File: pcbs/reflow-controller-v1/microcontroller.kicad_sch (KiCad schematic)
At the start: 15 parts, among them J3 SWD, J4 UART, U3 STM32G474VETx

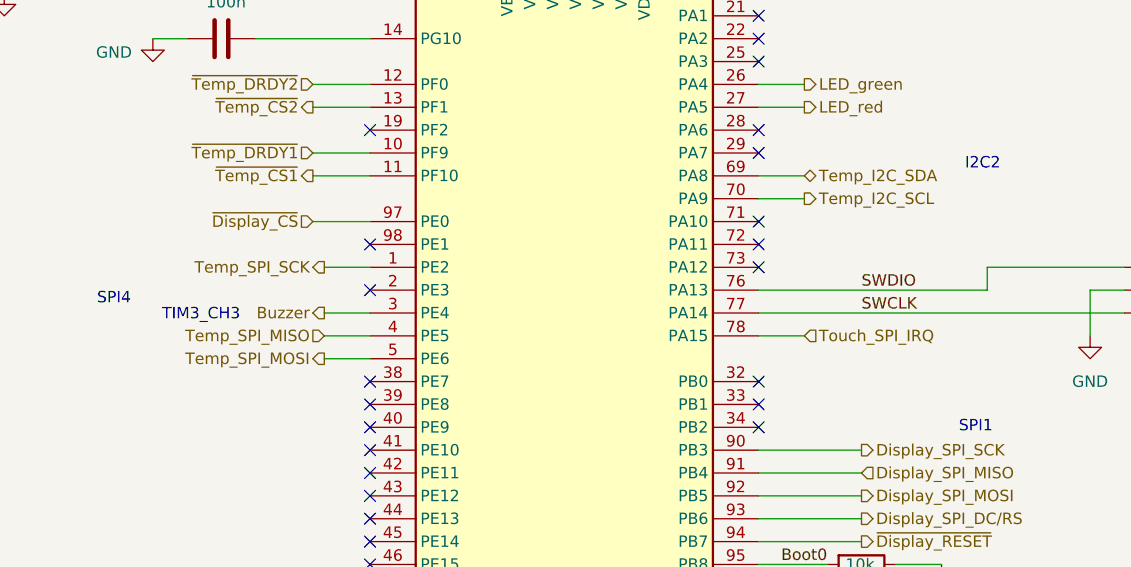
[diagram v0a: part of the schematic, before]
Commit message: move beeper
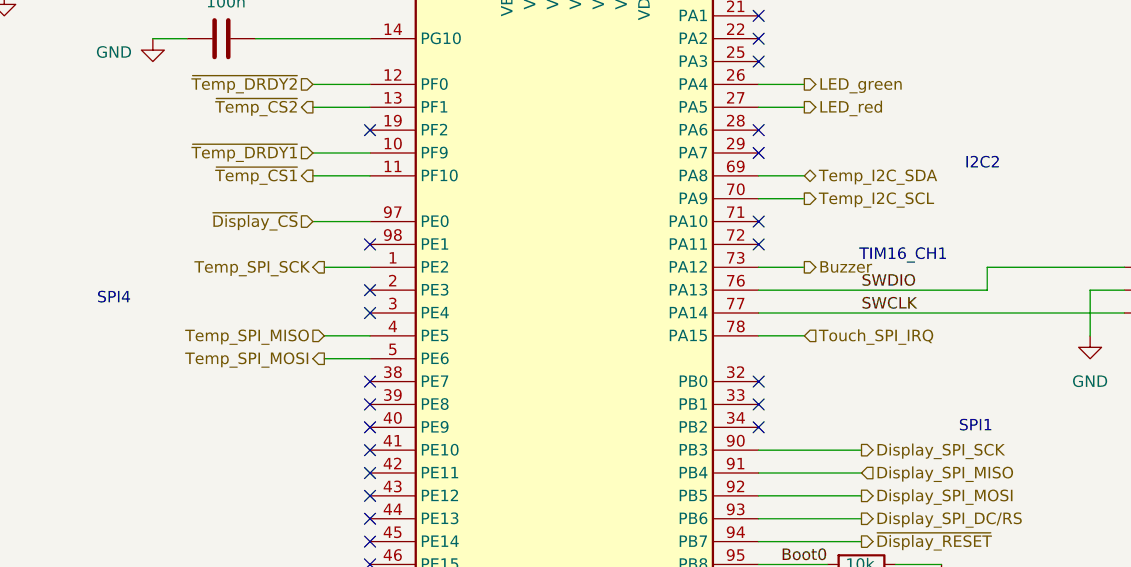
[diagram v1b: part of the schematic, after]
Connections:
- net Buzzer: now also U3.73 (PA12); no longer U3.3 (PE4)
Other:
- note added: "TIM16_CH1"
- note removed: "TIM3_CH3"
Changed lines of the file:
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@@
 	)
 	(no_connect
-		(at 144.78 69.85)
+		(at 101.6 74.93)
 	)
 	(no_connect
@@
 	(wire
 		(pts
-			(xy 96.52 74.93) (xy 101.6 74.93)
-		)
-		(stroke
-			(width 0)
-			(type default)
-		)
-	)
-	(wire
-		(pts
 			(xy 114.3 31.75) (xy 116.84 31.75)
 		)
@@
 	(wire
 		(pts
+			(xy 144.78 69.85) (xy 149.86 69.85)
+		)
+		(stroke
+			(width 0)
+			(type default)
+		)
+	)
+	(wire
+		(pts
 			(xy 101.6 140.97) (xy 93.98 140.97)
 		)
@@
 		)
 	)
-	(text "TIM3_CH3"
-		(exclude_from_sim no)
-		(at 78.486 75.184 0)
+	(text "TIM16_CH1"
+		(exclude_from_sim no)
+		(at 155.956 68.58 0)
 		(effects
 			(font
@@
 	(hierarchical_label "Buzzer"
 		(shape output)
-		(at 96.52 74.93 180)
-		(fields_autoplaced yes)
-		(effects
-			(font
-				(size 1.27 1.27)
-			)
-			(justify right)
-		)
-	)
+		(at 149.86 69.85 0)
+		(fields_autoplaced yes)
+		(effects
+			(font
+				(size 1.27 1.27)
+			)
+			(justify left)
+		)
+	)

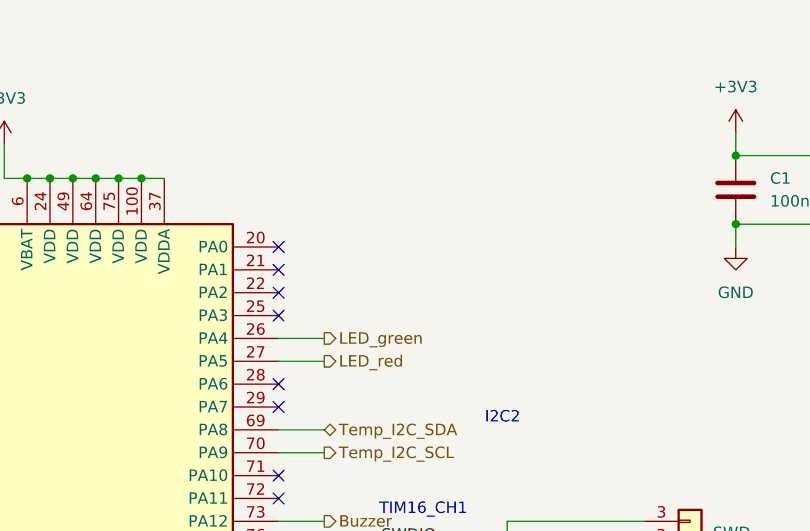
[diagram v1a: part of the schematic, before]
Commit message: add zero crossing detector
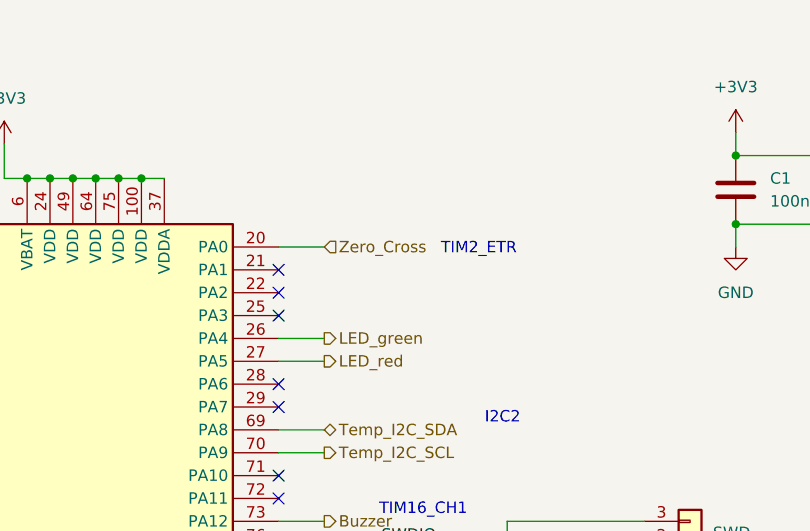
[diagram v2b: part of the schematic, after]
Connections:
- net Zero_Cross: now reaches U3.20 (PA0)
- no-connect marks 34 -> 33
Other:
- note added: "TIM2_ETR"
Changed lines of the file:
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@@
-	)
-	(no_connect
-		(at 144.78 39.37)
 	)
 	(no_connect
@@
 	(wire
 		(pts
+			(xy 144.78 39.37) (xy 149.86 39.37)
+		)
+		(stroke
+			(width 0)
+			(type default)
+		)
+	)
+	(wire
+		(pts
 			(xy 144.78 100.33) (xy 156.21 100.33)
 		)
@@
 				(size 1.27 1.27)
 			)
+		)
+	)
+	(text "TIM2_ETR"
+		(exclude_from_sim no)
+		(at 162.814 39.624 0)
+		(effects
+			(font
+				(size 1.27 1.27)
+			)
+			(justify left)
 		)
 	)
@@
 		)
 	)
+	(hierarchical_label "Zero_Cross"
+		(shape input)
+		(at 149.86 39.37 0)
+		(fields_autoplaced yes)
+		(effects
+			(font
+				(size 1.27 1.27)
+			)
+			(justify left)
+		)
+	)

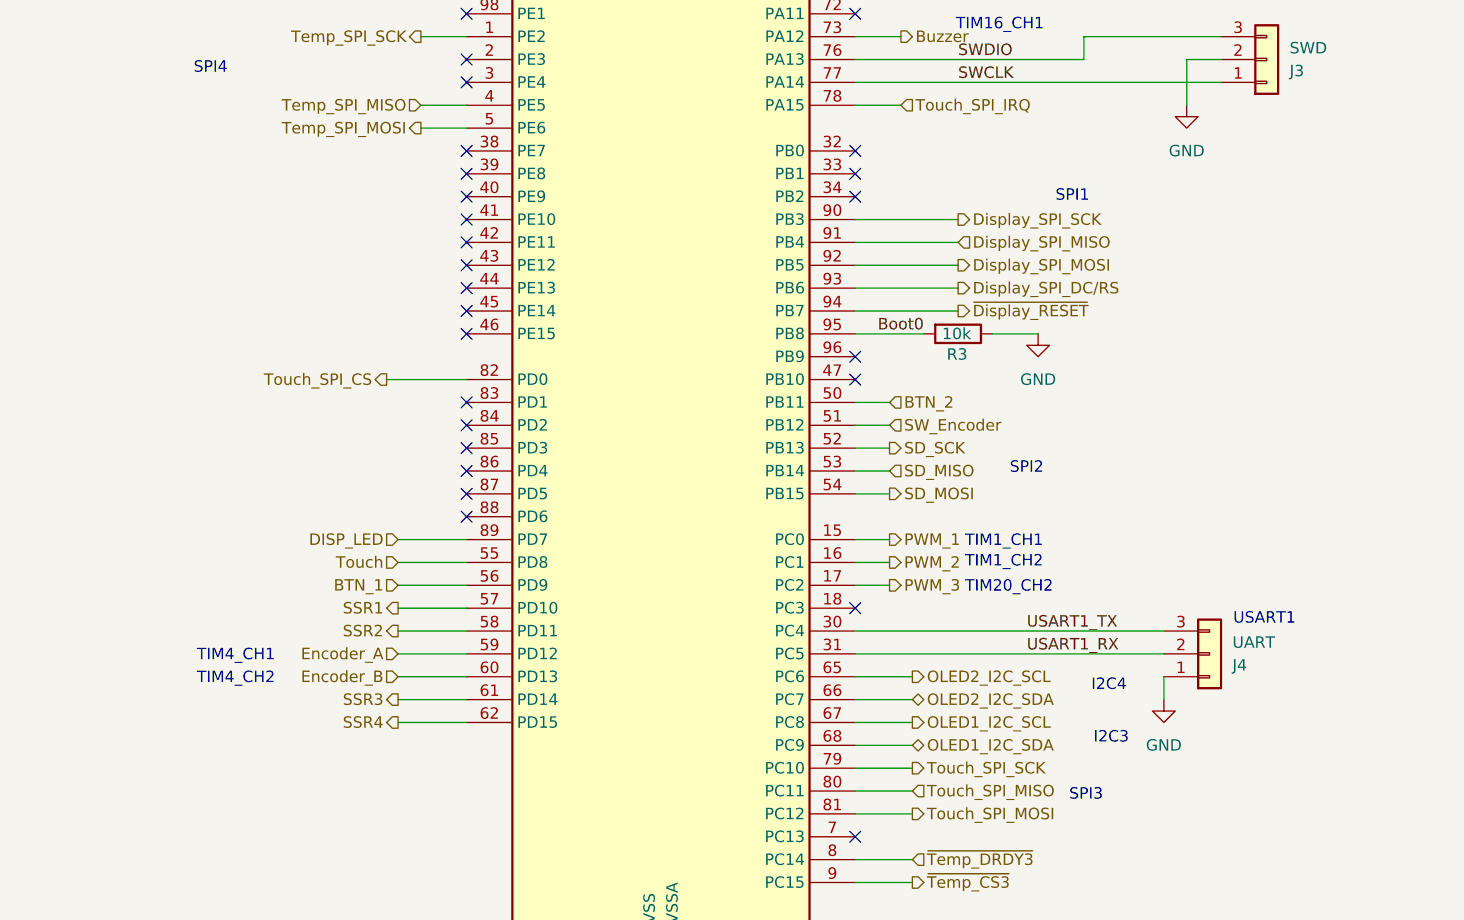
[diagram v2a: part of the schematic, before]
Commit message: update pcb size&display positioning
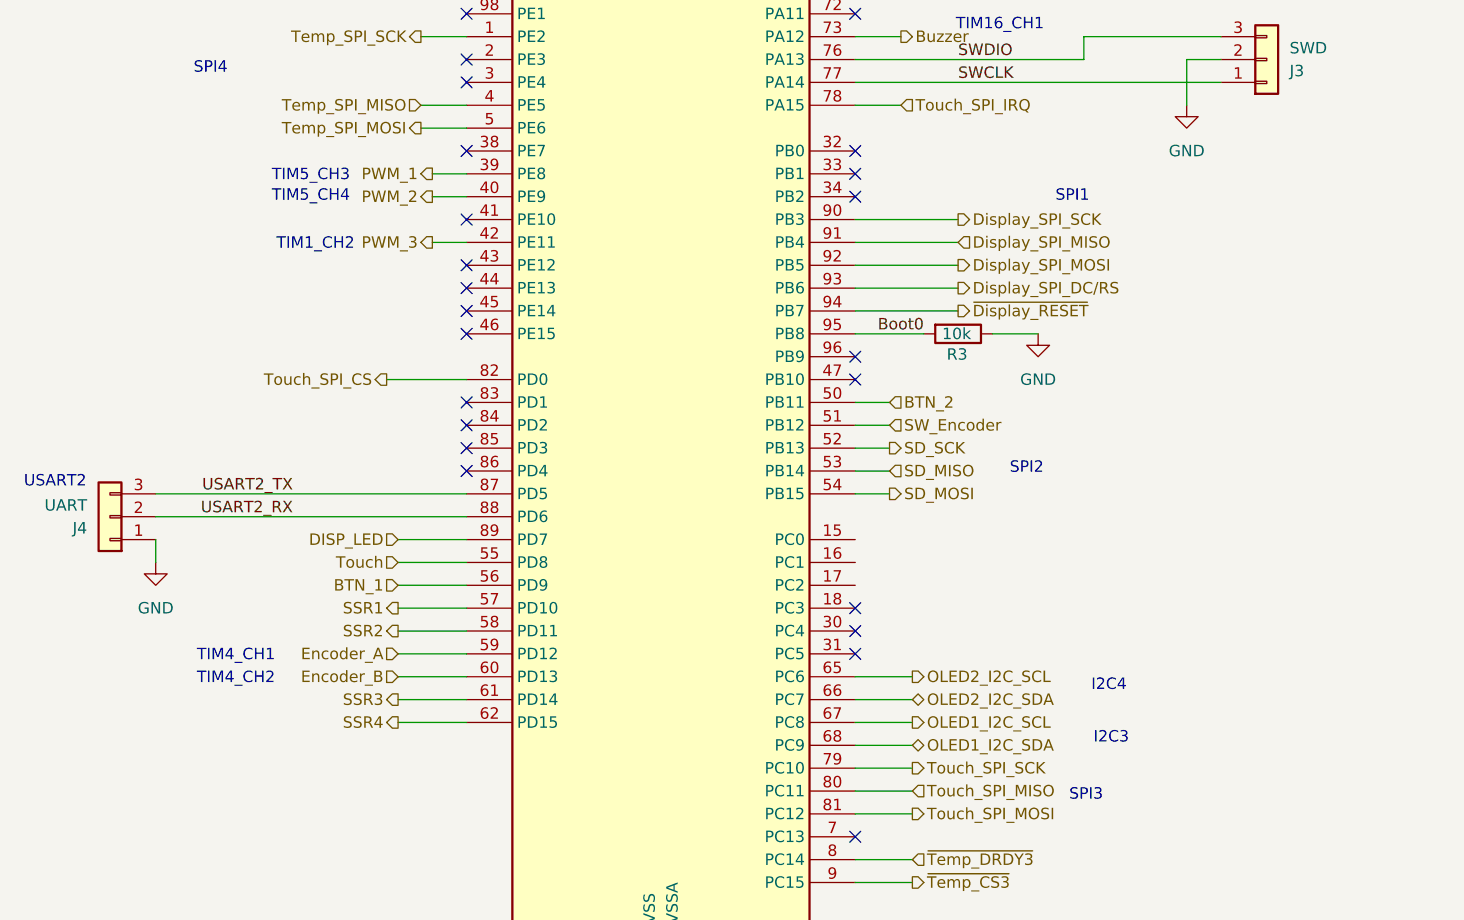
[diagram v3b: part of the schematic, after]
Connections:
- net PWM_1: now also U3.39 (PE8); no longer U3.15 (PC0)
- net PWM_2: now also U3.40 (PE9); no longer U3.16 (PC1)
- net PWM_3: now also U3.42 (PE11); no longer U3.17 (PC2)
- net USART2_TX: now reaches U3.87 (PD5)
- net USART2_TX: now also J4.3 (Pin_3)
- net USART2_RX: now reaches U3.88 (PD6)
- net USART2_RX: now also J4.2 (Pin_2)
- net USART1_RX: no longer names the net of U3.31 (PC5)
- net USART1_RX: no longer J4.2 (Pin_2)
- net USART1_TX: no longer names the net of U3.30 (PC4)
- net USART1_TX: no longer J4.3 (Pin_3)
- no-connect marks 33 -> 30
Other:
- note added: "TIM5_CH3"
- note added: "TIM5_CH4"
- note added: "USART2"
- note removed: "TIM1_CH1"
- note removed: "TIM20_CH2"
- note removed: "USART1"
- moved on the sheet: J4
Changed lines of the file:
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@@
-	)
-	(no_connect
-		(at 101.6 123.19)
 	)
 	(no_connect
@@
 	)
 	(no_connect
-		(at 101.6 85.09)
-	)
-	(no_connect
 		(at 101.6 100.33)
 	)
@@
 	)
 	(no_connect
-		(at 101.6 120.65)
-	)
-	(no_connect
 		(at 144.78 54.61)
 	)
@@
 	)
 	(no_connect
-		(at 101.6 92.71)
-	)
-	(no_connect
 		(at 144.78 46.99)
 	)
 	(no_connect
-		(at 101.6 87.63)
-	)
-	(no_connect
 		(at 144.78 107.95)
 	)
 	(no_connect
+		(at 144.78 135.89)
+	)
+	(no_connect
 		(at 101.6 82.55)
 	)
@@
 	)
 	(no_connect
+		(at 144.78 138.43)
+	)
+	(no_connect
 		(at 101.6 115.57)
 	)
@@
 	(wire
 		(pts
-			(xy 144.78 138.43) (xy 179.07 138.43)
+			(xy 67.056 123.19) (xy 101.6 123.19)
 		)
 		(stroke
@@
 	(wire
 		(pts
-			(xy 144.78 128.27) (xy 148.59 128.27)
+			(xy 101.6 87.63) (xy 97.79 87.63)
 		)
 		(stroke
@@
 	(wire
 		(pts
-			(xy 144.78 135.89) (xy 179.07 135.89)
+			(xy 67.056 120.65) (xy 101.6 120.65)
 		)
 		(stroke
@@
 	(wire
 		(pts
-			(xy 179.07 140.97) (xy 179.07 143.51)
+			(xy 67.056 125.73) (xy 67.056 128.27)
 		)
 		(stroke
@@
 	(wire
 		(pts
-			(xy 144.78 125.73) (xy 148.59 125.73)
+			(xy 101.6 85.09) (xy 97.79 85.09)
 		)
 		(stroke
@@
 	(wire
 		(pts
-			(xy 144.78 130.81) (xy 148.59 130.81)
+			(xy 101.6 92.71) (xy 97.79 92.71)
 		)
 		(stroke
@@
 		)
 	)
-	(text "TIM1_CH1"
+	(text "TIM5_CH3"
 		(exclude_from_sim no)
-		(at 156.972 125.984 0)
-		(effects
-			(font
-				(size 1.27 1.27)
-			)
-			(justify left)
+		(at 88.646 85.344 0)
+		(effects
+			(font
+				(size 1.27 1.27)
+			)
+			(justify right)
 		)
 	)
@@
 		)
 	)
-	(text "USART1"
+	(text "USART2"
 		(exclude_from_sim no)
-		(at 190.246 134.62 0)
-		(effects
-			(font
-				(size 1.27 1.27)
-			)
+		(at 55.88 119.38 0)
+		(effects
+			(font
+				(size 1.27 1.27)
+			)
+		)
+	)
+	(text "TIM5_CH4"
+		(exclude_from_sim no)
+		(at 88.646 87.63 0)
+		(effects
+			(font
+				(size 1.27 1.27)
+			)
+			(justify right)
 		)
 	)
 	(text "TIM1_CH2"
 		(exclude_from_sim no)
-		(at 156.972 128.27 0)
-		(effects
-			(font
-				(size 1.27 1.27)
-			)
-			(justify left)
-		)
-	)
-	(text "TIM20_CH2"
-		(exclude_from_sim no)
-		(at 156.972 131.064 0)
-		(effects
-			(font
-				(size 1.27 1.27)
-			)
-			(justify left)
-		)
-	)
-	(label "USART1_RX"
-		(at 163.83 138.43 0)
-		(fields_autoplaced yes)
-		(effects
-			(font
-				(size 1.27 1.27)
-			)
-			(justify left bottom)
-		)
-	)
-	(label "USART1_TX"
-		(at 163.83 135.89 0)
-		(fields_autoplaced yes)
-		(effects
-			(font
-				(size 1.27 1.27)
-			)
-			(justify left bottom)
+		(at 89.154 92.964 0)
+		(effects
+			(font
+				(size 1.27 1.27)
+			)
+			(justify right)
+		)
+	)
+	(label "USART2_RX"
+		(at 82.296 123.19 180)
+		(fields_autoplaced yes)
+		(effects
+			(font
+				(size 1.27 1.27)
+			)
+			(justify right bottom)
+		)
+	)
+	(label "USART2_TX"
+		(at 82.296 120.65 180)
+		(fields_autoplaced yes)
+		(effects
+			(font
+				(size 1.27 1.27)
+			)
+			(justify right bottom)
 		)
 	)
@@
 	(hierarchical_label "PWM_3"
 		(shape output)
-		(at 148.59 130.81 0)
-		(fields_autoplaced yes)
-		(effects
-			(font
-				(size 1.27 1.27)
-			)
-			(justify left)
+		(at 97.79 92.71 180)
+		(fields_autoplaced yes)
+		(effects
+			(font
+				(size 1.27 1.27)
+			)
+			(justify right)
 		)
 	)
@@
 	(hierarchical_label "PWM_2"
 		(shape output)
-		(at 148.59 128.27 0)
-		(fields_autoplaced yes)
-		(effects
-			(font
-				(size 1.27 1.27)
-			)
-			(justify left)
+		(at 97.79 87.63 180)
+		(fields_autoplaced yes)
+		(effects
+			(font
+				(size 1.27 1.27)
+			)
+			(justify right)
 		)
 	)
@@
 	(hierarchical_label "PWM_1"
 		(shape output)
-		(at 148.59 125.73 0)
-		(fields_autoplaced yes)
-		(effects
-			(font
-				(size 1.27 1.27)
-			)
-			(justify left)
+		(at 97.79 85.09 180)
+		(fields_autoplaced yes)
+		(effects
+			(font
+				(size 1.27 1.27)
+			)
+			(justify right)
 		)
 	)
@@
 	(symbol
 		(lib_id "power:GND")
-		(at 179.07 143.51 0)
+		(at 67.056 128.27 0)
+		(mirror y)
 		(unit 1)
 		(exclude_from_sim no)
@@
 		(fields_autoplaced yes)
 		(property "Reference" "#PWR019"
-			(at 179.07 149.86 0)
+			(at 67.056 134.62 0)
 			(effects
 				(font
@@
 		)
 		(property "Value" "GND"
-			(at 179.07 148.59 0)
+			(at 67.056 133.35 0)
 			(effects
 				(font
@@
 		)
 		(property "Footprint" ""
-			(at 179.07 143.51 0)
+			(at 67.056 128.27 0)
 			(effects
 				(font
@@
 		)
 		(property "Datasheet" ""
-			(at 179.07 143.51 0)
+			(at 67.056 128.27 0)
 			(effects
 				(font
@@
 		)
 		(property "Description" "Power symbol creates a global label with name \"GND\" , ground"
-			(at 179.07 143.51 0)
+			(at 67.056 128.27 0)
 			(effects
 				(font
@@
 	(symbol
 		(lib_id "Connector_Generic:Conn_01x03")
-		(at 184.15 138.43 0)
-		(mirror x)
+		(at 61.976 123.19 180)
 		(unit 1)
 		(exclude_from_sim no)
@@
 		(dnp no)
 		(property "Reference" "J4"
-			(at 186.69 139.7001 0)
+			(at 59.436 124.4601 0)
 			(effects
 				(font
@@
 		)
 		(property "Value" "UART"
-			(at 186.69 137.1601 0)
+			(at 59.436 121.9201 0)
 			(effects
 				(font
@@
 		)
 		(property "Footprint" "Connector_Molex:Molex_KK-254_AE-6410-03A_1x03_P2.54mm_Vertical"
-			(at 184.15 138.43 0)
+			(at 61.976 123.19 0)
 			(effects
 				(font
@@
 		)
 		(property "Datasheet" "~"
-			(at 184.15 138.43 0)
+			(at 61.976 123.19 0)
 			(effects
 				(font
@@
 		)
 		(property "Description" "Generic connector, single row, 01x03, script generated (kicad-library-utils/schlib/autogen/connector/)"
-			(at 184.15 138.43 0)
-			(effects
-				(font
+			(at 61.976 123.19 0)
+			(effects
+				(font
